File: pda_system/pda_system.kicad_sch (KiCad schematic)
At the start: 7 parts, among them J1 Screw_Terminal_01x04, U1 STM32F103C8Tx, U2 SN65HVD230, U3 MP2303ADP, Y1 Crystal

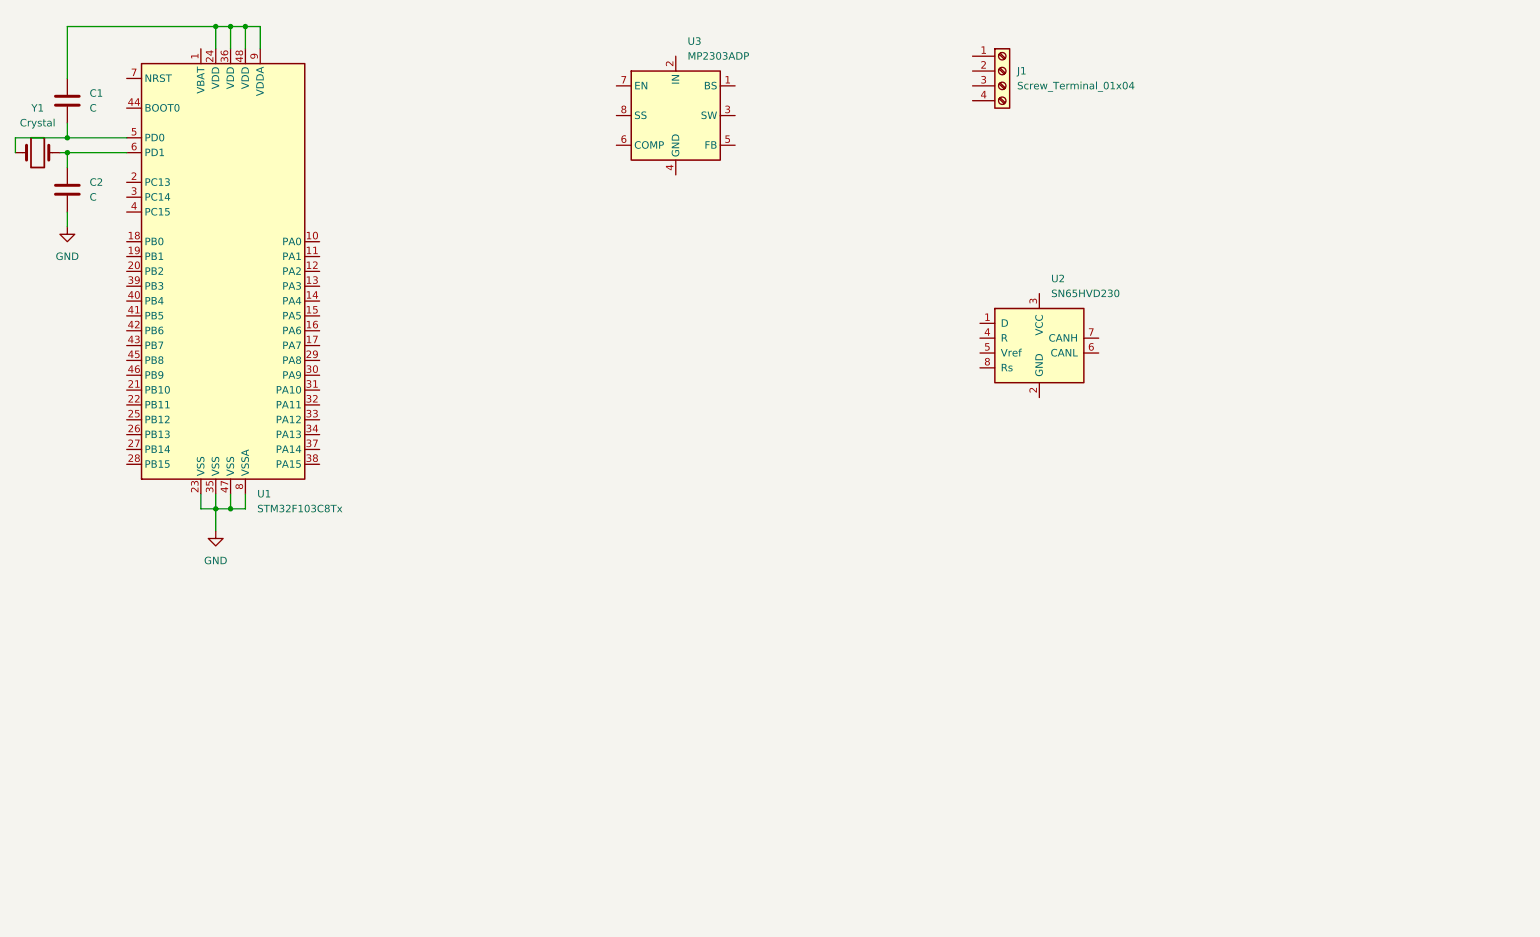
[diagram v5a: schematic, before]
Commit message: updated with correct componets for the power/buck converter
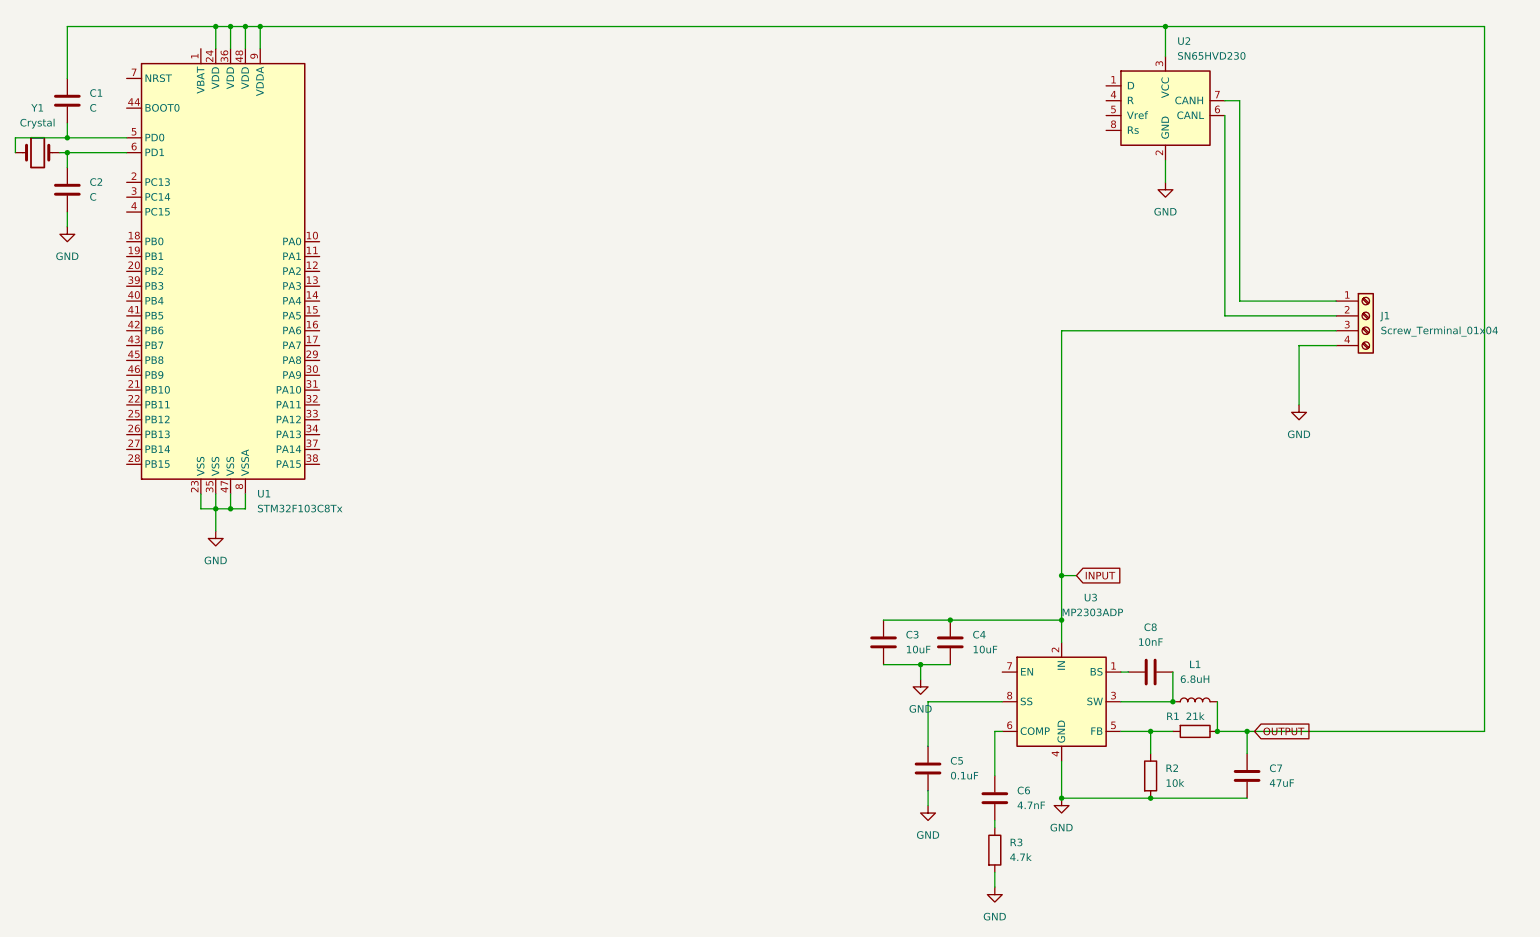
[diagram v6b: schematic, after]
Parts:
- added C3, C4: 10uF, symbol Device:C
- added C5: 0.1uF, symbol Device:C
- added C6: 4.7nF, symbol Device:C
- added C7: 47uF, symbol Device:C
- added C8: 10nF, symbol Device:C
- added L1: 6.8uH, symbol Device:L
- added R1: 21k, symbol Device:R
- added R2: 10k, symbol Device:R
- added R3: 4.7k, symbol Device:R
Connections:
- net GND: now also J1.4 (Pin_4), U2.2 (GND), U3.4 (GND), C3.2, C4.2, C5.2, C7.2, R2.2, R3.2
- net at U3.1 (BS): now also C8.2
- net INPUT: now reaches U3.2 (IN)
- net INPUT: now also J1.3 (Pin_3), C3.1, C4.1
- net at U3.3 (SW): now also C8.1, L1.1
- net at U3.5 (FB): now also R1.2, R2.1
- net at U3.6 (COMP): now also C6.1
- net at U3.8 (SS): now also C5.1
- net OUTPUT: now reaches C1.1, U1.24 (VDD), U1.36 (VDD), U1.48 (VDD), U1.9 (VDDA)
- net OUTPUT: now also U2.3 (VCC), C7.1, L1.2, R1.1
- net at U2.6 (CANL): now also J1.2 (Pin_2)
- net at U2.7 (CANH): now also J1.1 (Pin_1)
- new net: C6.2, R3.1
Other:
- moved on the sheet: J1, U2, U3

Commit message: updated with annotations and comments for blocks
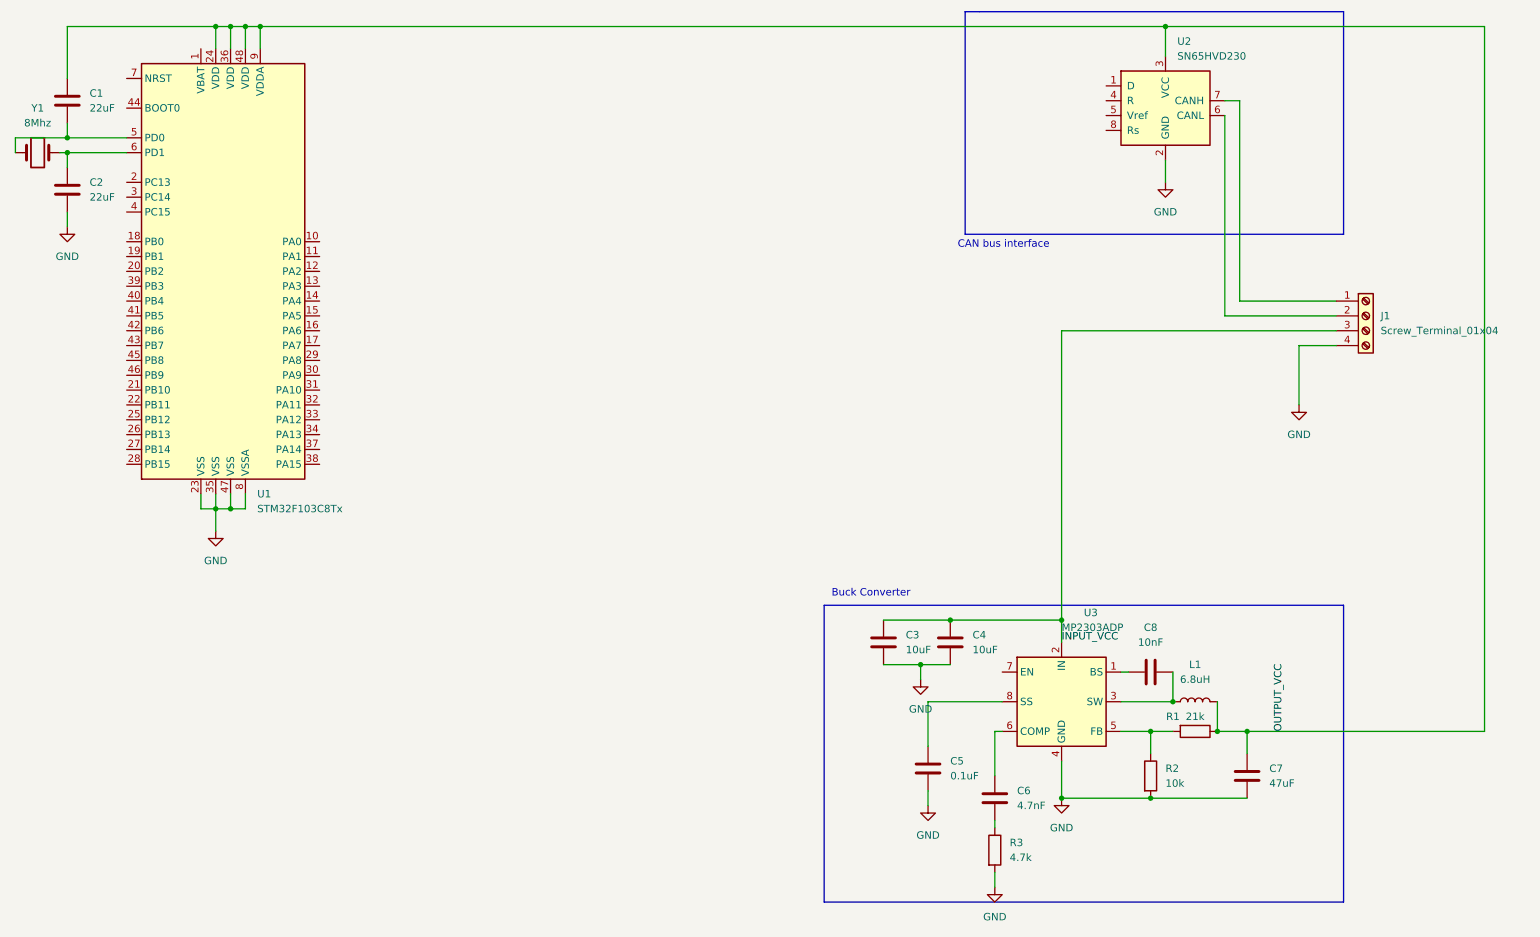
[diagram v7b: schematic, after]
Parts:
- C1, C2: value C -> 22uF
- Y1: value Crystal -> 8Mhz
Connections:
- net INPUT renamed INPUT_VCC
- net OUTPUT renamed OUTPUT_VCC
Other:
- note added: "Buck Converter"
- note added: "CAN bus interface"
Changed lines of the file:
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@@
   (junction (at 205.74 116.84) (diameter 0) (color 0 0 0 0)
   )
-  (junction (at 205.74 109.22) (diameter 0) (color 0 0 0 0)
-  )
   (junction (at 232.41 135.89) (diameter 0) (color 0 0 0 0)
   )
@@
     (stroke (width 0) (type default) (color 0 0 0 0))
   )
+  (polyline (pts (xy 254 165.1) (xy 165.1 165.1))
+    (stroke (width 0) (type default) (color 0 0 0 0))
+  )
   (wire (pts (xy 195.58 130.81) (xy 182.88 130.81))
     (stroke (width 0) (type default) (color 0 0 0 0))
@@
     (stroke (width 0) (type default) (color 0 0 0 0))
   )
+  (polyline (pts (xy 191.77 12.7) (xy 254 12.7))
+    (stroke (width 0) (type default) (color 0 0 0 0))
+  )
   (wire (pts (xy 26.67 34.29) (xy 26.67 36.83))
     (stroke (width 0) (type default) (color 0 0 0 0))
@@
     (stroke (width 0) (type default) (color 0 0 0 0))
   )
-  (wire (pts (xy 205.74 109.22) (xy 205.74 116.84))
+  (wire (pts (xy 205.74 67.31) (xy 205.74 116.84))
     (stroke (width 0) (type default) (color 0 0 0 0))
   )
@@
     (stroke (width 0) (type default) (color 0 0 0 0))
   )
-  (wire (pts (xy 205.74 109.22) (xy 208.28 109.22))
-    (stroke (width 0) (type default) (color 0 0 0 0))
-  )
   (wire (pts (xy 35.56 36.83) (xy 45.72 36.83))
     (stroke (width 0) (type default) (color 0 0 0 0))
@@
     (stroke (width 0) (type default) (color 0 0 0 0))
   )
+  (polyline (pts (xy 254 114.3) (xy 254 165.1))
+    (stroke (width 0) (type default) (color 0 0 0 0))
+  )
   (wire (pts (xy 246.38 69.85) (xy 246.38 80.01))
     (stroke (width 0) (type default) (color 0 0 0 0))
@@
     (stroke (width 0) (type default) (color 0 0 0 0))
   )
+  (polyline (pts (xy 254 12.7) (xy 254 50.8))
+    (stroke (width 0) (type default) (color 0 0 0 0))
+  )
   (wire (pts (xy 66.04 97.79) (xy 63.5 97.79))
     (stroke (width 0) (type default) (color 0 0 0 0))
   )
+  (polyline (pts (xy 254 50.8) (xy 189.23 50.8))
+    (stroke (width 0) (type default) (color 0 0 0 0))
+  )
   (wire (pts (xy 66.04 95.25) (xy 66.04 97.79))
     (stroke (width 0) (type default) (color 0 0 0 0))
   )
+  (polyline (pts (xy 189.23 12.7) (xy 191.77 12.7))
+    (stroke (width 0) (type default) (color 0 0 0 0))
+  )
+  (polyline (pts (xy 165.1 165.1) (xy 165.1 114.3))
+    (stroke (width 0) (type default) (color 0 0 0 0))
+  )
   (wire (pts (xy 68.58 15.24) (xy 66.04 15.24))
     (stroke (width 0) (type default) (color 0 0 0 0))
@@
     (stroke (width 0) (type default) (color 0 0 0 0))
   )
+  (polyline (pts (xy 165.1 114.3) (xy 254 114.3))
+    (stroke (width 0) (type default) (color 0 0 0 0))
+  )
   (wire (pts (xy 45.72 34.29) (xy 35.56 34.29))
     (stroke (width 0) (type default) (color 0 0 0 0))
@@
     (stroke (width 0) (type default) (color 0 0 0 0))
   )
-  (wire (pts (xy 205.74 67.31) (xy 205.74 109.22))
-    (stroke (width 0) (type default) (color 0 0 0 0))
-  )
   (wire (pts (xy 66.04 15.24) (xy 63.5 15.24))
     (stroke (width 0) (type default) (color 0 0 0 0))
@@
     (stroke (width 0) (type default) (color 0 0 0 0))
   )
+  (polyline (pts (xy 189.23 50.8) (xy 189.23 12.7))
+    (stroke (width 0) (type default) (color 0 0 0 0))
+  )
   (wire (pts (xy 215.9 125.73) (xy 217.17 125.73))
     (stroke (width 0) (type default) (color 0 0 0 0))
   )
-  (global_label "INPUT" (shape input) (at 208.28 109.22 0) (fields_autoplaced)
-    (effects (font (size 1.27 1.27)) (justify left))
-    (property "Intersheet References" "${INTERSHEET_REFS}" (id 0) (at 216.1964 109.1406 0)
-      (effects (font (size 1.27 1.27)) (justify left) hide)
-    )
-  )
-  (global_label "OUTPUT" (shape input) (at 238.76 135.89 0) (fields_autoplaced)
-    (effects (font (size 1.27 1.27)) (justify left))
-    (property "Intersheet References" "${INTERSHEET_REFS}" (id 0) (at 248.3698 135.8106 0)
-      (effects (font (size 1.27 1.27)) (justify left) hide)
-    )
+  (text "CAN bus interface" (at 187.96 53.34 0)
+    (effects (font (size 1.27 1.27)) (justify left bottom))
+  )
+  (text "Buck Converter" (at 166.37 113.03 0)
+    (effects (font (size 1.27 1.27)) (justify left bottom))
+  )
+  (label "OUTPUT_VCC" (at 243.84 135.89 90)
+    (effects (font (size 1.27 1.27)) (justify left bottom))
+  )
+  (label "INPUT_VCC" (at 205.74 120.65 0)
+    (effects (font (size 1.27 1.27)) (justify left bottom))
   )
   (symbol (lib_id "Device:C") (at 35.56 43.18 0) (unit 1)
@@
       (effects (font (size 1.27 1.27)) (justify left))
     )
-    (property "Value" "C" (id 1) (at 39.37 44.4499 0)
+    (property "Value" "22uF" (id 1) (at 39.37 44.4499 0)
       (effects (font (size 1.27 1.27)) (justify left))
     )
@@
   (symbol (lib_id "Regulator_Switching:MP2303ADP") (at 205.74 130.81 0) (unit 1)
     (in_bom yes) (on_board yes)
-    (property "Reference" "U3" (id 0) (at 209.55 113.03 0)
-      (effects (font (size 1.27 1.27)) (justify left))
-    )
-    (property "Value" "MP2303ADP" (id 1) (at 205.74 115.57 0)
+    (property "Reference" "U3" (id 0) (at 209.55 115.57 0)
+      (effects (font (size 1.27 1.27)) (justify left))
+    )
+    (property "Value" "MP2303ADP" (id 1) (at 205.74 118.11 0)
       (effects (font (size 1.27 1.27)) (justify left))
     )
@@
     (in_bom yes) (on_board yes) (fields_autoplaced)
     (property "Reference" "Y1" (id 0) (at 30.48 29.21 0))
-    (property "Value" "Crystal" (id 1) (at 30.48 31.75 0))
+    (property "Value" "8Mhz" (id 1) (at 30.48 31.75 0))
     (property "Footprint" "Crystal:Crystal_HC49-4H_Vertical" (id 2) (at 30.48 36.83 0)
       (effects (font (size 1.27 1.27)) hide)
@@
       (effects (font (size 1.27 1.27)) (justify left))
     )
-    (property "Value" "C" (id 1) (at 39.37 29.2099 0)
+    (property "Value" "22uF" (id 1) (at 39.37 29.2099 0)
       (effects (font (size 1.27 1.27)) (justify left))
     )
@@
     )
     (path "/e4b930d4-e153-4821-a72c-c924db7df444"
-      (reference "C1") (unit 1) (value "C") (footprint "")
+      (reference "C1") (unit 1) (value "22uF") (footprint "")
     )
     (path "/065f4e5e-6a63-4d78-b2c5-cfc02e75af73"
-      (reference "C2") (unit 1) (value "C") (footprint "")
+      (reference "C2") (unit 1) (value "22uF") (footprint "")
     )
     (path "/c9c9839e-d43e-401e-b0e9-81c64e18cd8f"
@@
     )
     (path "/7550a2ff-4cfd-4300-8cc1-1407b01c45e0"
-      (reference "Y1") (unit 1) (value "Crystal") (footprint "Crystal:Crystal_HC49-4H_Vertical")
-    )
-  )
+      (reference "Y1") (unit 1) (value "8Mhz") (footprint "Crystal:Crystal_HC49-4H_Vertical")
+    )
+  )

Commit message: updated with schematic page comments/title
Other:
- company: (none) -> None
- title: (none) -> PDA_sensor_module
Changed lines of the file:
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@@
 (kicad_sch (version 20211123) (generator eeschema)
   (paper "A4")
+  (title_block
+    (title "PDA_sensor_module")
+    (date "2023-11-16")
+    (rev "0.0.1")
+    (company "None")
+    (comment 1 "First revision of data logging sensor module")
+  )
   (junction (at 60.96 15.24) (diameter 0) (color 0 0 0 0)
   )
